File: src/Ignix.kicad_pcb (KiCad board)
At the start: 2 copper layers, 63.2 x 63.2 mm, 16 parts, among them M1 Motor_DC, Q1 NPN, Q2 PNP, SW1 SW_Push

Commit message: revised repo
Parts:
- removed R2: 47kΩ, Resistor_THT:R_Axial_DIN0207_L6.3mm_D2.5mm_P7.62mm_Horizontal
- added G***: LOGO, LOGO, B.Cu at (127.1, 89.8)
- moved G*** 3.20 mm to (99.3, 90.2)
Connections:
- M1 pad 1: Net-(D1-A) -> Net-(M1-+)
- M1 pad 2: Net-(BT1-+) -> Net-(D1-A)
- Q2 pad 1: Net-(D1-A) -> Net-(M1-+)
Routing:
- net Net-(M1-+): track 0.00 -> 49.4 mm, vias 0 -> 1
- net Net-(BT1-+): track 118.8 -> 78.5 mm, vias 3 -> 0
- net Net-(D1-A): track 69.6 -> 46.7 mm, vias 1 -> 0
- net Net-(R1-Pad2): track 31.3 -> 20.4 mm
- net Net-(Q1-B): track 51.3 -> 42.8 mm
- net Net-(C1-Pad1): track 55.4 -> 61.1 mm
- net Net-(Q1-C): track 32.3 -> 36.7 mm
- net Net-(BT1--): track 70.3 -> 72.2 mm, vias 0 -> 3
- net Net-(Q2-B): track 16.1 -> 17.9 mm
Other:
- board text added: "V1"

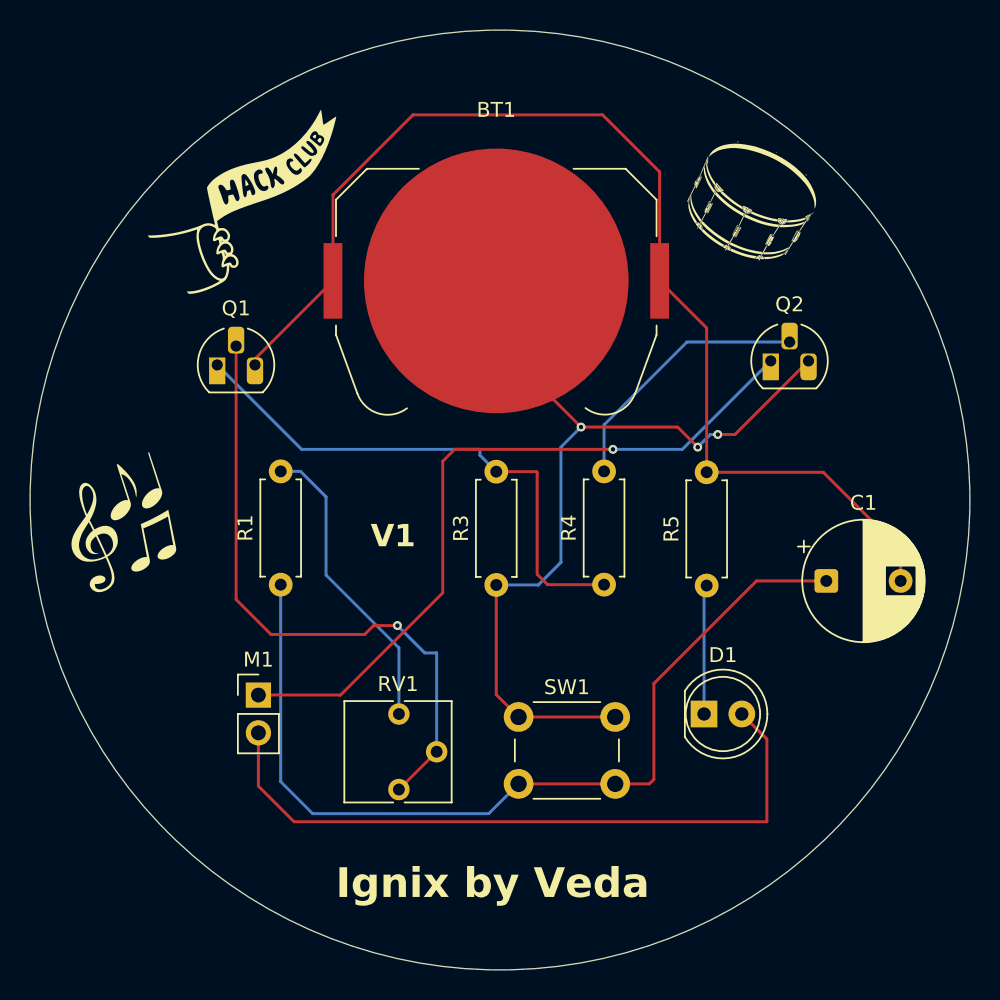
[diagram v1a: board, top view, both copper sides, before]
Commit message: flipped battery
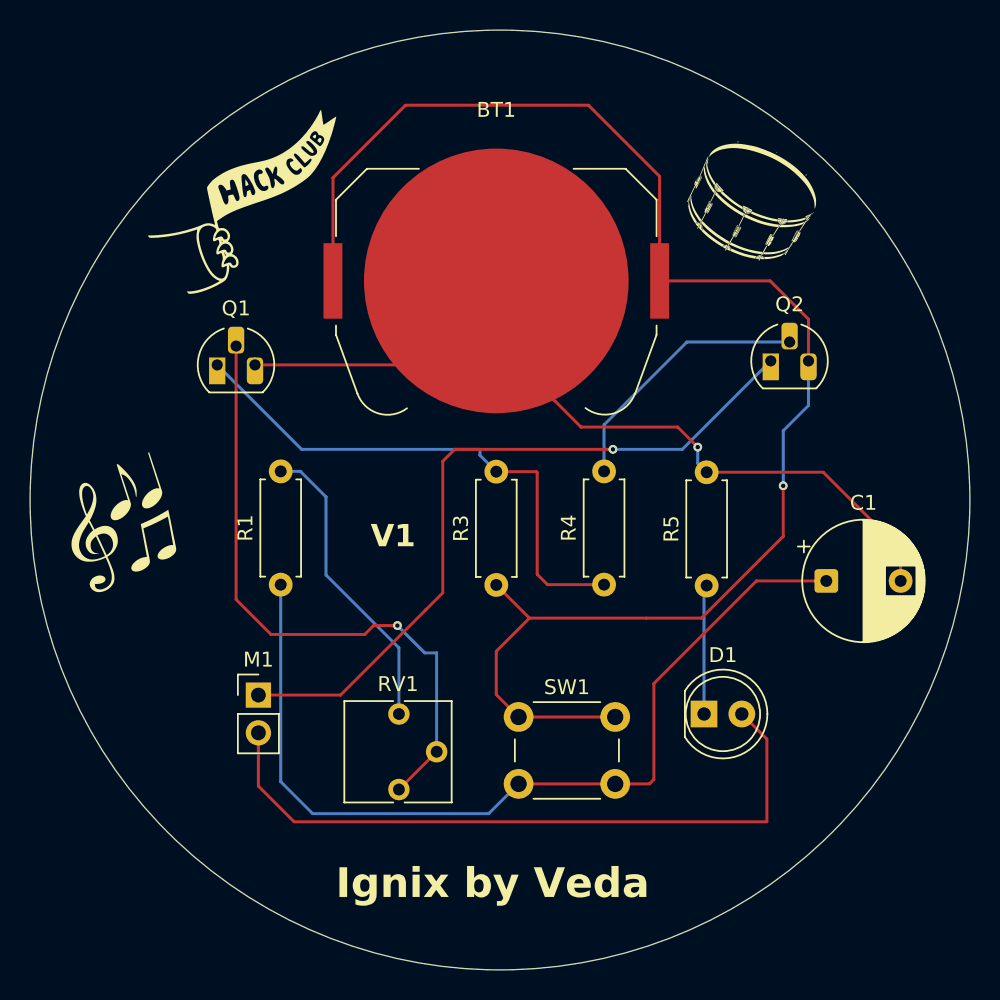
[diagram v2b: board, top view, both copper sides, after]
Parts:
- moved G*** 0.70 mm to (127.0, 89.1)
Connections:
- C1 pad 2: Net-(BT1-+) -> Net-(BT1--)
- Q1 pad 3: Net-(BT1-+) -> Net-(BT1--)
- Q2 pad 3: Net-(BT1--) -> Net-(BT1-+)
- R3 pad 1: Net-(BT1--) -> Net-(BT1-+)
- R5 pad 2: Net-(BT1-+) -> Net-(BT1--)
- SW1 pad 1: Net-(BT1--) -> Net-(BT1-+)
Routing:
- net Net-(BT1-+): track 78.5 -> 104.4 mm, vias 0 -> 1
- net Net-(BT1--): track 72.2 -> 69.7 mm, vias 3 -> 1
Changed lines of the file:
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@@
 			(layers "*.Cu" "*.Mask")
 			(remove_unused_layers no)
-			(net 2 "Net-(BT1--)")
+			(net 1 "Net-(BT1-+)")
 			(pintype "passive")
 		)
@@
 			(layers "*.Cu" "*.Mask")
 			(remove_unused_layers no)
-			(net 1 "Net-(BT1-+)")
+			(net 2 "Net-(BT1--)")
 			(pintype "passive")
 		)
@@
 			(remove_unused_layers no)
 			(roundrect_rratio 0.25)
-			(net 2 "Net-(BT1--)")
+			(net 1 "Net-(BT1-+)")
 			(pinfunction "E")
 			(pintype "open_emitter")
@@
 			(remove_unused_layers no)
 			(roundrect_rratio 0.25)
-			(net 1 "Net-(BT1-+)")
+			(net 2 "Net-(BT1--)")
 			(pinfunction "E")
 			(pintype "open_emitter")
@@
 			(layers "*.Cu" "*.Mask")
 			(remove_unused_layers no)
-			(net 2 "Net-(BT1--)")
+			(net 1 "Net-(BT1-+)")
 			(pinfunction "1")
 			(pintype "passive")
@@
 			(layers "*.Cu" "*.Mask")
 			(remove_unused_layers no)
-			(net 2 "Net-(BT1--)")
+			(net 1 "Net-(BT1-+)")
 			(pinfunction "1")
 			(pintype "passive")
@@
 			(layers "*.Cu" "*.Mask")
 			(remove_unused_layers no)
-			(net 1 "Net-(BT1-+)")
+			(net 2 "Net-(BT1--)")
 			(pintype "passive")
 		)
@@
 	(footprint "LOGO"
 		(layer "B.Cu")
-		(at 127.11 89.84 180)
+		(at 127.04153 89.144438 180)
 		(property "Reference" "G***"
 			(at 0 0 0)
@@
 	)
 	(segment
-		(start 151.897349 94)
-		(end 151.897349 91.897349)
+		(start 134.8 96.5)
+		(end 138.5 96.5)
 		(width 0.2)
 		(layer "F.Cu")
@@
 	)
 	(segment
-		(start 108.47 79.47)
-		(end 108.47 79.06375)
+		(start 145.7 76.4)
+		(end 143.11875 73.81875)
 		(width 0.2)
 		(layer "F.Cu")
@@
 	)
 	(segment
-		(start 108.47 79.06375)
-		(end 113.715 73.81875)
+		(start 124.7 98.73)
+		(end 126.93 96.5)
 		(width 0.2)
 		(layer "F.Cu")
@@
 	)
 	(segment
-		(start 119.1 62.65)
-		(end 131.85 62.65)
+		(start 124.7 101.65)
+		(end 126.2 103.15)
 		(width 0.2)
 		(layer "F.Cu")
@@
 	)
 	(segment
-		(start 146.69 86.69)
-		(end 138.85 86.69)
+		(start 145.7 79.2)
+		(end 145.7 76.4)
 		(width 0.2)
 		(layer "F.Cu")
@@
 	)
 	(segment
-		(start 151.897349 91.897349)
-		(end 146.69 86.69)
+		(start 124.7 101.65)
+		(end 124.7 98.73)
 		(width 0.2)
 		(layer "F.Cu")
@@
 	)
 	(segment
-		(start 131.85 62.65)
-		(end 135.685 66.485)
+		(start 143.11875 73.81875)
+		(end 135.685 73.81875)
 		(width 0.2)
 		(layer "F.Cu")
@@
 	)
 	(segment
-		(start 135.685 66.485)
-		(end 135.685 73.81875)
+		(start 145.9 79)
+		(end 145.7 79.2)
 		(width 0.2)
 		(layer "F.Cu")
@@
 	)
 	(segment
-		(start 138.85 86.69)
-		(end 138.85 76.98375)
+		(start 124.7 94.27)
+		(end 126.93 96.5)
 		(width 0.2)
 		(layer "F.Cu")
@@
 	)
 	(segment
-		(start 113.715 68.035)
-		(end 119.1 62.65)
+		(start 126.93 96.5)
+		(end 134.8 96.5)
 		(width 0.2)
 		(layer "F.Cu")
@@
 	)
 	(segment
-		(start 135.685 74.135)
+		(start 138.5 96.5)
+		(end 142.4 92.6)
+		(width 0.2)
+		(layer "F.Cu")
+		(net 1)
+	)
+	(segment
+		(start 135.685 66.785)
 		(end 135.685 73.81875)
 		(width 0.2)
@@
 	)
 	(segment
-		(start 113.715 73.81875)
-		(end 113.715 68.035)
+		(start 144 91)
+		(end 144 87.6)
 		(width 0.2)
 		(layer "F.Cu")
@@
 	)
 	(segment
-		(start 138.85 76.98375)
+		(start 113.715 66.885)
+		(end 118.6 62)
+		(width 0.2)
+		(layer "F.Cu")
+		(net 1)
+	)
+	(segment
+		(start 135.685 74.135)
 		(end 135.685 73.81875)
 		(width 0.2)
@@
 	)
 	(segment
-		(start 138.25 85)
-		(end 136.9 83.65)
+		(start 113.715 73.81875)
+		(end 113.715 66.885)
 		(width 0.2)
 		(layer "F.Cu")
-		(net 2)
+		(net 1)
 	)
 	(segment
-		(start 130.4 83.65)
-		(end 124.7 77.95)
+		(start 142.4 92.6)
+		(end 144 91)
 		(width 0.2)
 		(layer "F.Cu")
-		(net 2)
+		(net 1)
 	)
 	(segment
-		(start 145.7 79.2)
-		(end 140.75 84.15)
+		(start 118.6 62)
+		(end 130.9 62)
 		(width 0.2)
 		(layer "F.Cu")
-		(net 2)
+		(net 1)
 	)
 	(segment
-		(start 124.7 77.95)
-		(end 124.7 73.81875)
+		(start 126.2 103.15)
+		(end 132.7 103.15)
 		(width 0.2)
 		(layer "F.Cu")
-		(net 2)
+		(net 1)
 	)
 	(segment
-		(start 136.9 83.65)
-		(end 130.4 83.65)
+		(start 130.9 62)
+		(end 135.685 66.785)
 		(width 0.2)
 		(layer "F.Cu")
-		(net 2)
+		(net 1)
+	)
+	(via
+		(at 144 87.6)
+		(size 0.6)
+		(drill 0.3)
+		(layers "F.Cu" "B.Cu")
+		(net 1)
 	)
 	(segment
-		(start 145.9 79)
+		(start 144 83.9)
+		(end 145.7 82.2)
+		(width 0.2)
+		(layer "B.Cu")
+		(net 1)
+	)
+	(segment
+		(start 145.5 79.4)
 		(end 145.7 79.2)
 		(width 0.2)
-		(layer "F.Cu")
-		(net 2)
+		(layer "B.Cu")
+		(net 1)
 	)
 	(segment
-		(start 124.7 73.81875)
-		(end 128.83125 77.95)
+		(start 144 87.6)
+		(end 144 83.9)
 		(width 0.2)
-		(layer "F.Cu")
-		(net 2)
+		(layer "B.Cu")
+		(net 1)
 	)
 	(segment
-		(start 126.2 103.15)
-		(end 124.7 101.65)
+		(start 145.7 82.2)
+		(end 145.7 79.2)
+		(width 0.2)
+		(layer "B.Cu")
+		(net 1)
+	)
+	(segment
+		(start 138.25 85)
+		(end 136.9 83.65)
 		(width 0.2)
 		(layer "F.Cu")
@@
 	)
 	(segment
-		(start 128.25 77.36875)
-		(end 124.7 73.81875)
+		(start 151.897349 94)
+		(end 151.897349 91.897349)
 		(width 0.2)
 		(layer "F.Cu")
@@
 	)
 	(segment
-		(start 126.2 103.15)
-		(end 132.7 103.15)
+		(start 108.47 79.47)
+		(end 108.47 79.06375)
 		(width 0.2)
 		(layer "F.Cu")
@@
 	)
 	(segment
-		(start 124.7 101.65)
-		(end 124.7 94.27)
+		(start 130.4 83.65)
+		(end 124.7 77.95)
 		(width 0.2)
 		(layer "F.Cu")
@@
 	)
 	(segment
-		(start 140.75 84.15)
-		(end 139.6 84.15)
+		(start 119.04875 79.47)
+		(end 124.7 73.81875)
 		(width 0.2)
 		(layer "F.Cu")
 		(net 2)
 	)
-	(via
-		(at 138.25 85)
-		(size 0.6)
-		(drill 0.3)
-		(layers "F.Cu" "B.Cu")
+	(segment
+		(start 146.69 86.69)
+		(end 138.85 86.69)
+		(width 0.2)
+		(layer "F.Cu")
 		(net 2)
 	)
-	(via
-		(at 130.4 83.65)
-		(size 0.6)
-		(drill 0.3)
-		(layers "F.Cu" "B.Cu")
+	(segment
+		(start 124.7 77.95)
+		(end 124.7 73.81875)
+		(width 0.2)
+		(layer "F.Cu")
 		(net 2)
 	)
-	(via
-		(at 139.6 84.15)
-		(size 0.6)
-		(drill 0.3)
-		(layers "F.Cu" "B.Cu")
+	(segment
+		(start 136.9 83.65)
+		(end 130.4 83.65)
+		(width 0.2)
+		(layer "F.Cu")
 		(net 2)
 	)
 	(segment
-		(start 139.1 84.15)
-		(end 138.25 85)
+		(start 108.47 79.47)
+		(end 119.04875 79.47)
 		(width 0.2)
-		(layer "B.Cu")
+		(layer "F.Cu")
 		(net 2)
 	)
 	(segment
-		(start 124.7 94.27)
-		(end 127.53 94.27)
+		(start 151.897349 91.897349)
+		(end 146.69 86.69)
 		(width 0.2)
-		(layer "B.Cu")
+		(layer "F.Cu")
 		(net 2)
 	)
 	(segment
-		(start 129.05 85)
-		(end 130.4 83.65)
+		(start 124.7 73.81875)
+		(end 128.83125 77.95)
 		(width 0.2)
-		(layer "B.Cu")
+		(layer "F.Cu")
 		(net 2)
 	)
 	(segment
-		(start 127.53 94.27)
-		(end 129.05 92.75)
+		(start 128.25 77.36875)
+		(end 124.7 73.81875)
 		(width 0.2)
-		(layer "B.Cu")
+		(layer "F.Cu")
+		(net 2)
+	)
+	(via
+		(at 138.25 85)
+		(size 0.6)
+		(drill 0.3)
+		(layers "F.Cu" "B.Cu")
 		(net 2)
 	)
 	(segment
-		(start 129.05 92.75)
-		(end 129.05 85)
+		(start 138.25 85)
+		(end 138.25 86.09)
 		(width 0.2)
 		(layer "B.Cu")
@@
 	)
 	(segment
-		(start 139.6 84.15)
-		(end 139.1 84.15)
+		(start 138.25 86.09)
+		(end 138.85 86.69)
 		(width 0.2)
 		(layer "B.Cu")
